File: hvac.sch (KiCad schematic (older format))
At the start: 5 parts

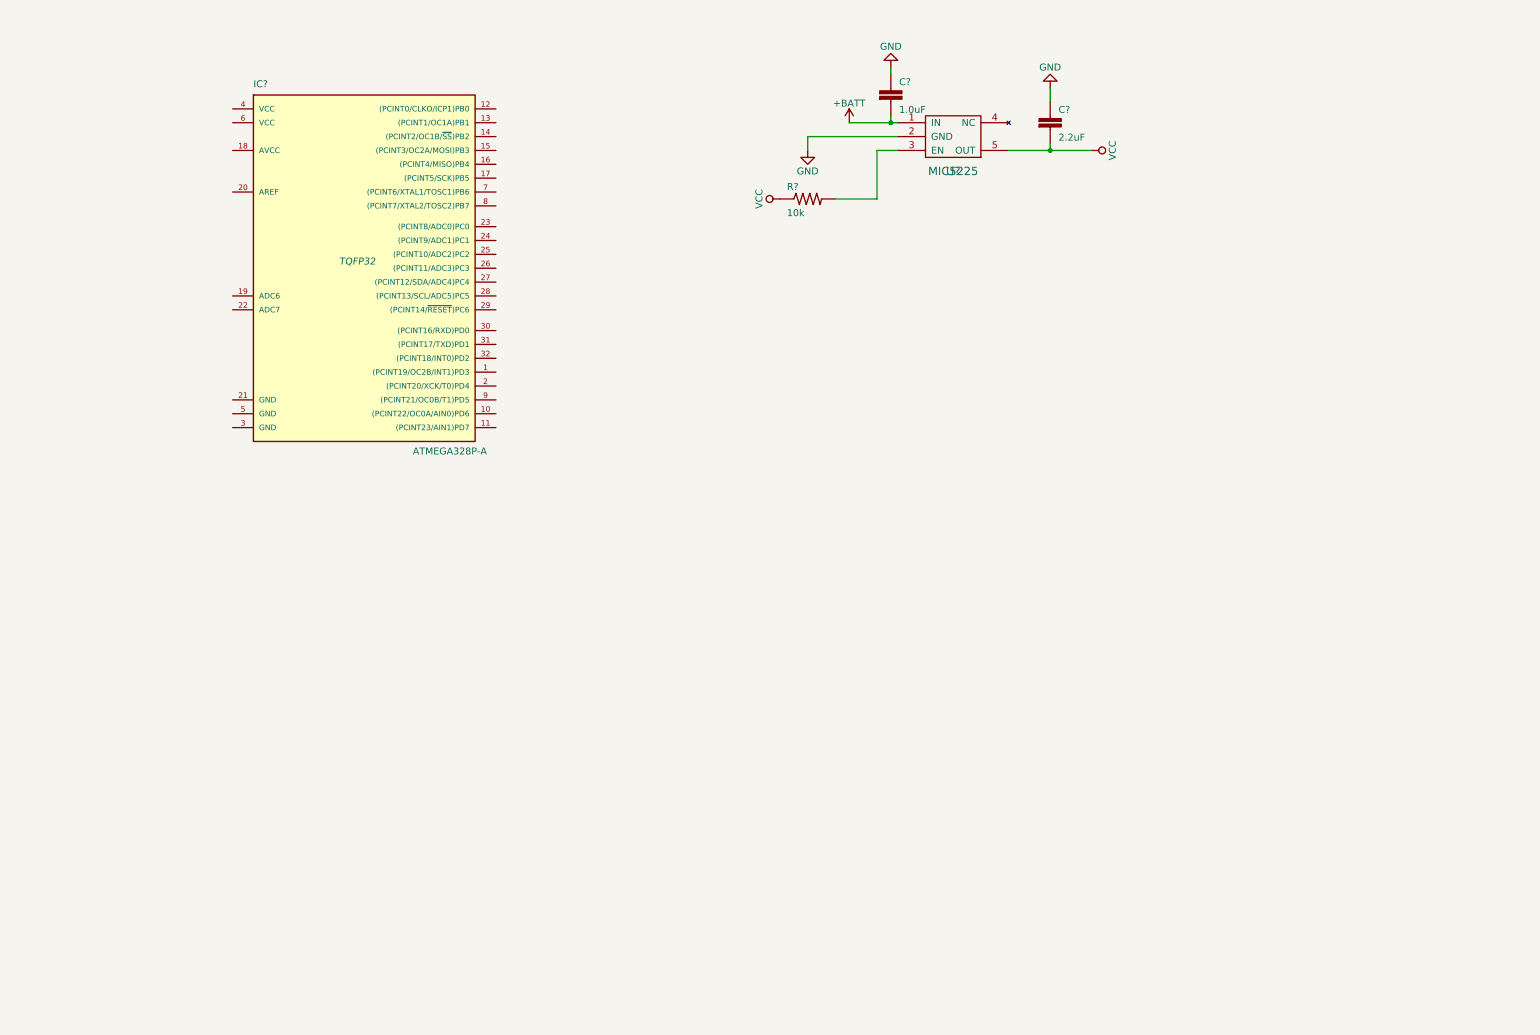
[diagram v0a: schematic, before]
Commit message: Add components
 *  Add power supply
 *  Add LEDs
 *  Add Serial
 *  Add programming header
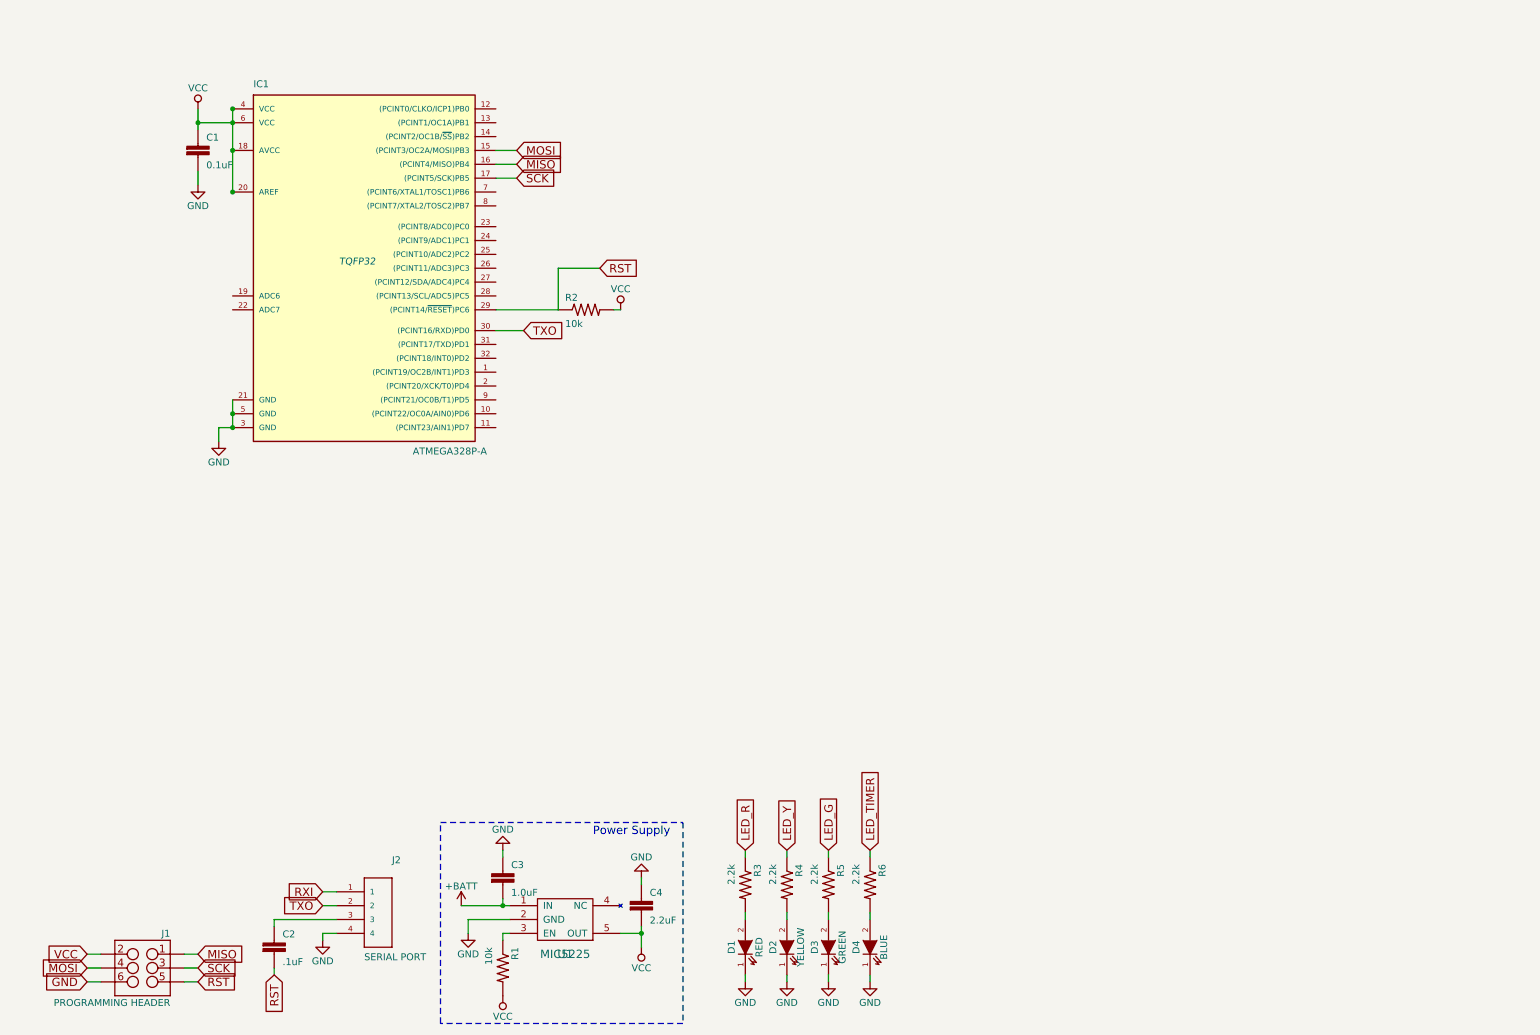
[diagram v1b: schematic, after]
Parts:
- added C1: 0.1uF, 0603-CAP, symbol CAP0603-CAP
- added C2: .1uF, 0603-CAP, symbol CAP0603-CAP
- added D1: RED, symbol LED
- added D2: YELLOW, symbol LED
- added D3: GREEN, symbol LED
- added D4: BLUE, symbol LED
- added J1: PROGRAMMING HEADER, 2X3, symbol M03X22X3_SILK_MALE_PTH
- added J2: SERIAL PORT, 1X04-3.5MM, symbol 1X4-3.5MM
- added R2: 10k, 0402-RES, symbol RESISTOR0402
- added R3, R4, R5, R6: 2.2k, 0402-RES, symbol RESISTOR0402
- gave numbers to parts that had none: 5
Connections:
- net GND: now also IC1.21 (GND), IC1.3 (GND), IC1.5 (GND), C1.2, D1.1 (K), D2.1 (K), D3.1 (K), D4.1 (K), J1.6, J2.4
- net VCC: now also IC1.18 (AVCC), IC1.20 (AREF), IC1.4 (VCC), IC1.6 (VCC), R1.2, C1.1, J1.2, R2.2; no longer R1.1
- net MOSI: now reaches IC1.15 ((PCINT3/OC2A/MOSI)PB3)
- net MOSI: now also J1.4
- net MISO: now reaches IC1.16 ((PCINT4/MISO)PB4)
- net MISO: now also J1.1
- net SCK: now reaches IC1.17 ((PCINT5/SCK)PB5)
- net SCK: now also J1.3
- net RST: now reaches IC1.29 ((PCINT14/~RESET~)PC6)
- net RST: now also C2.2, J1.5, R2.1
- net TXO: now reaches IC1.30 ((PCINT16/RXD)PD0)
- net TXO: now also J2.2
- net at U1.3 (EN): now also R1.1; no longer R1.2
- new net: C2.1, J2.3
- new net: D1.2 (A), R3.2
- new net: D2.2 (A), R4.2
- new net: D3.2 (A), R5.2
- new net: D4.2 (A), R6.2
- new net LED_G: R5.1
- new net LED_R: R3.1
- new net LED_TIMER: R6.1
- new net LED_Y: R4.1
- new net RXI: J2.1
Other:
- note added: "Power Supply"
- moved on the sheet: C3, C4, R1, U1

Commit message: Wire up inputs and outputs
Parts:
- added BTN1, SW1, SW2, SW3: SPST, symbol SPST
- added D5: BLUE, symbol LED
- added R7: 2.2k, 0402-RES, symbol RESISTOR0402
- added R8, R9: 1k, 0402-RES, symbol RESISTOR0402
- added RV1, RV2: POT, symbol POT
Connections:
- net GND: now also D5.1 (K), R8.2, R9.2, SW1.1, SW2.1, SW3.1
- net LED_G: now also IC1.2 ((PCINT20/XCK/T0)PD4)
- net LED_R: now also IC1.31 ((PCINT17/TXD)PD1)
- net LED_TIMER: now also IC1.11 ((PCINT23/AIN1)PD7)
- net LED_Y: now also IC1.32 ((PCINT18/INT0)PD2)
- net VCC: now also RV1.1, RV2.1
- net OUT_SWAMP_FAN: now reaches IC1.1 ((PCINT19/OC2B/INT1)PD3)
- net OUT_PUMP: now reaches IC1.10 ((PCINT22/OC0A/AIN0)PD6)
- net SW_SWAMP: now reaches IC1.12 ((PCINT0/CLKO/ICP1)PB0)
- net SW_SWAMP: now also SW1.2
- net SW_VENT_OVERRIDE: now reaches IC1.13 ((PCINT1/OC1A)PB1)
- net SW_AUTOVENT: now reaches IC1.14 ((PCINT2/OC1B/~SS~)PB2)
- net SW_AUTOVENT: now also SW3.2
- net POT_VENT_SPEED: now reaches IC1.19 (ADC6)
- net POT_VENT_SPEED: now also RV1.2
- net POT_TEMP_DIFF: now reaches IC1.22 (ADC7)
- net POT_TEMP_DIFF: now also RV2.2
- net BATTERY_VOLTAGE_DIVIDER: now reaches IC1.25 ((PCINT10/ADC2)PC2)
- net SW_WATER_LIMIT: now reaches IC1.26 ((PCINT11/ADC3)PC3)
- net LED_WATER_LIMIT: now reaches IC1.27 ((PCINT12/SDA/ADC4)PC4)
- net LED_WATER_LIMIT: now also R7.1
- net BTN_TIMER: now reaches IC1.28 ((PCINT13/SCL/ADC5)PC5)
- net BTN_TIMER: now also BTN1.2
- net TEMP_OUTSIDE: now reaches IC1.7 ((PCINT6/XTAL1/TOSC1)PB6)
- net TEMP_INSIDE: now reaches IC1.8 ((PCINT7/XTAL2/TOSC2)PB7)
- net OUT_VENT_FAN: now reaches IC1.9 ((PCINT21/OC0B/T1)PD5)
- new net: R9.1, RV1.3
- new net: R8.1, RV2.3
- new net: D5.2 (A), R7.2
- new net SW_VENT_OVERRIIDE: SW2.2
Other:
- moved on the sheet: D1, D2, D3, D4, R2, R3, R4, R5, R6

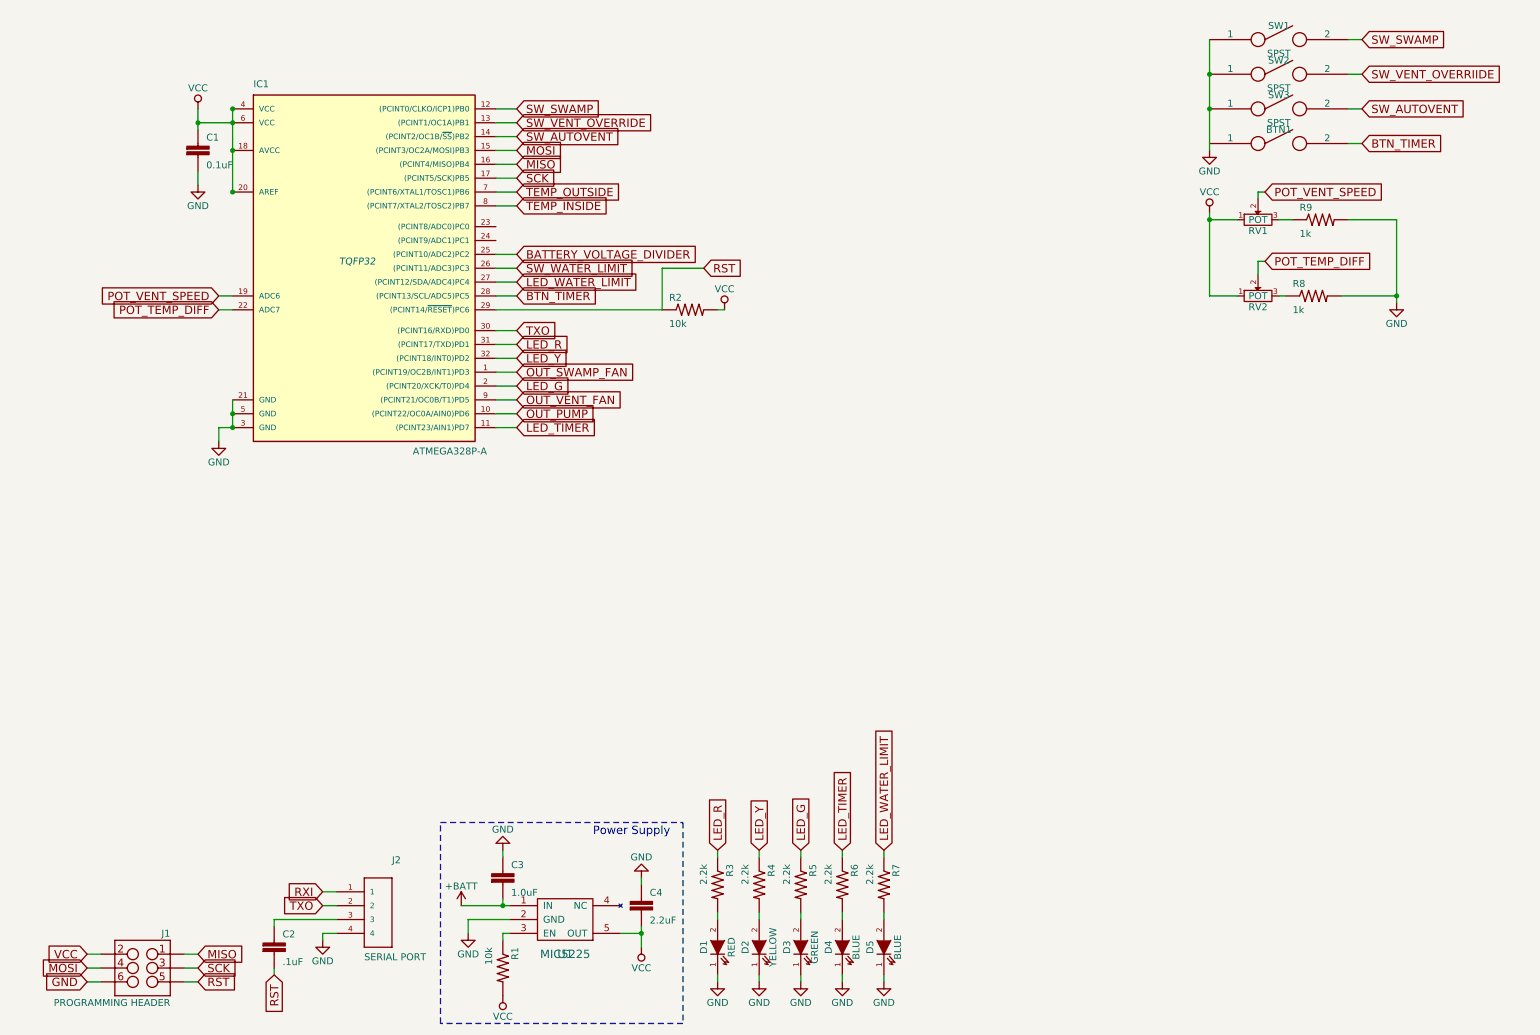
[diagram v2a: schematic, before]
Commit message: Hook up all components and fix warnings
TODO: Set up output stages
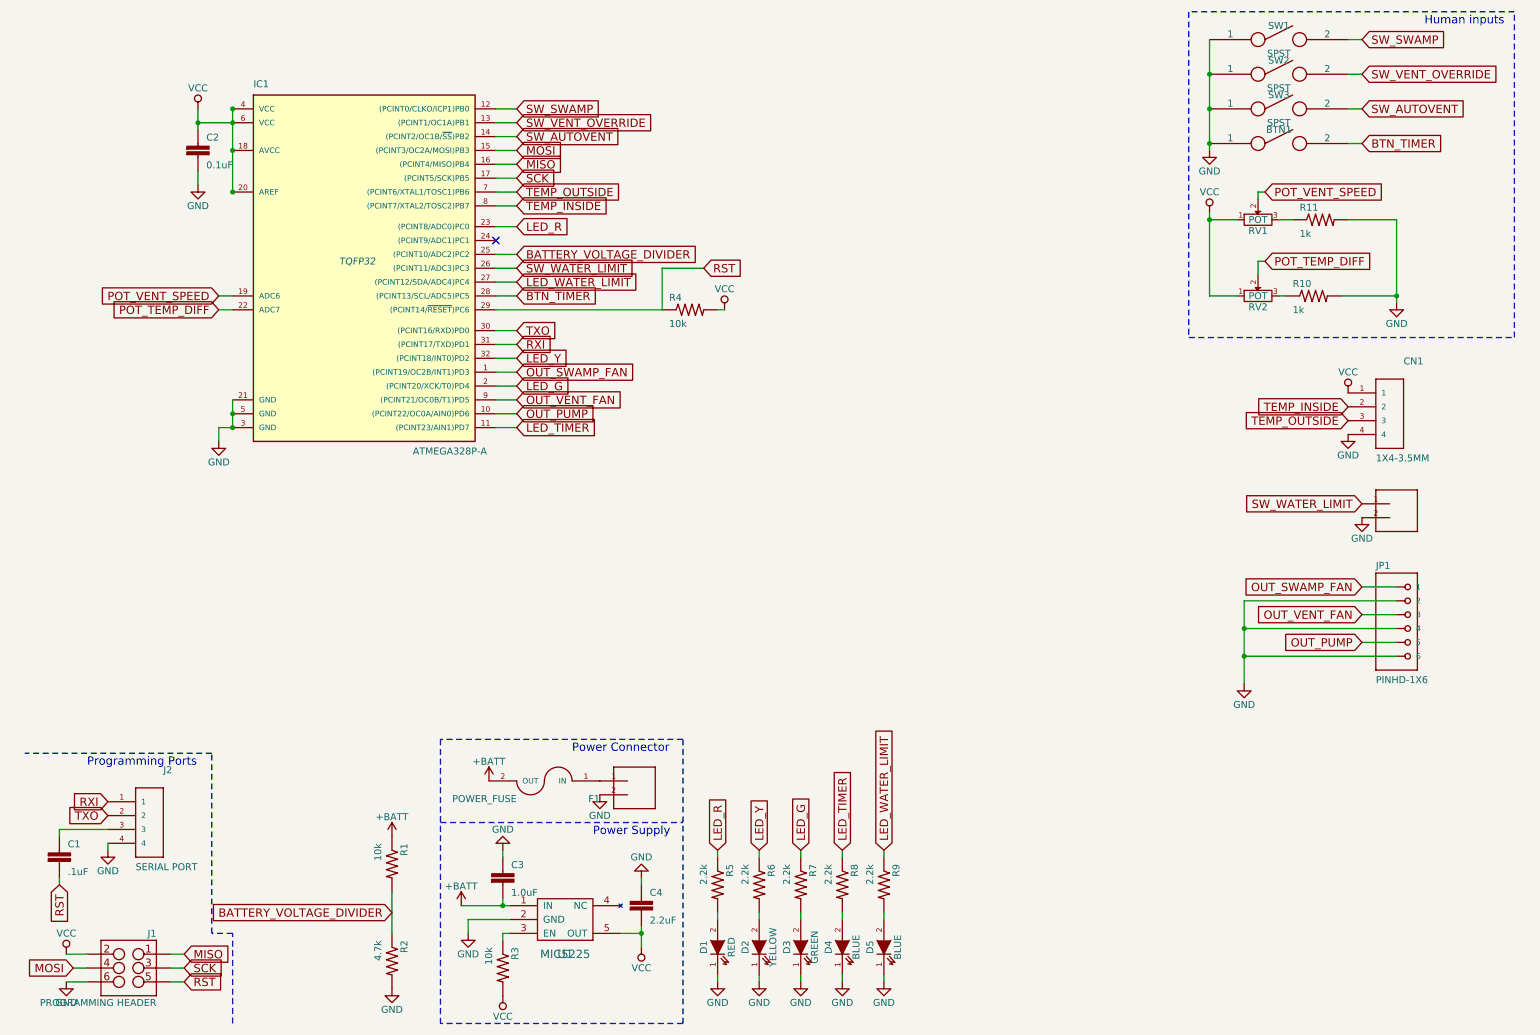
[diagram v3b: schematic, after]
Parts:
- added CN1: 1X4-3.5MM, 1X04-3.5MM, symbol 1X4-3.5MM
- added F1: POWER_FUSE, FUSE_5MM, symbol POWER_FUSE
- added J3: POWER_INPUT, 1X2-3.5MM, symbol POWER_INPUT
- added J4: 1X2-3.5MM, 1X2-3.5MM, symbol 1X2-3.5MM
- added JP1: PINHD-1X6, 1X06, symbol PINHD-1X6
- added R1: 10k, 0402-RES, symbol RESISTOR0402
- added R2: 4.7k, 0402-RES, symbol RESISTOR0402
- renumbered C2 to C1, C1 to C2, R8 to R10, R9 to R11, R1 to R3, R2 to R4, R3 to R5, R4 to R6, R5 to R7, R6 to R8, R7 to R9
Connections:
- net SW_VENT_OVERRIIDE is gone; now on net SW_VENT_OVERRIDE: SW2.2
- net +BATT: now also F1.2 (OUT), R1.1
- net BATTERY_VOLTAGE_DIVIDER: now also R1.2, R2.1
- net GND: now also BTN1.1, CN1.4, J3.2, J4.2, JP1.2, JP1.4, JP1.6, R2.2
- net LED_R: now also IC1.23 ((PCINT8/ADC0)PC0); no longer IC1.31 ((PCINT17/TXD)PD1)
- net OUT_PUMP: now also JP1.5
- net OUT_SWAMP_FAN: now also JP1.1
- net OUT_VENT_FAN: now also JP1.3
- net RXI: now also IC1.31 ((PCINT17/TXD)PD1)
- net SW_WATER_LIMIT: now also J4.1
- net TEMP_INSIDE: now also CN1.2
- net TEMP_OUTSIDE: now also CN1.3
- net VCC: now also CN1.1
- new net: F1.1 (IN), J3.1
- no-connect marks 0 -> 1
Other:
- note added: "Human inputs"
- note added: "Power Connector"
- note added: "Programming Ports"
- moved on the sheet: C1, J1, J2
